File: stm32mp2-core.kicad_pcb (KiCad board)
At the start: 2 copper layers, 2 parts, among them U1 STM32MP257FAI3, U2 MT53E1G32D2FW-046 IT:B

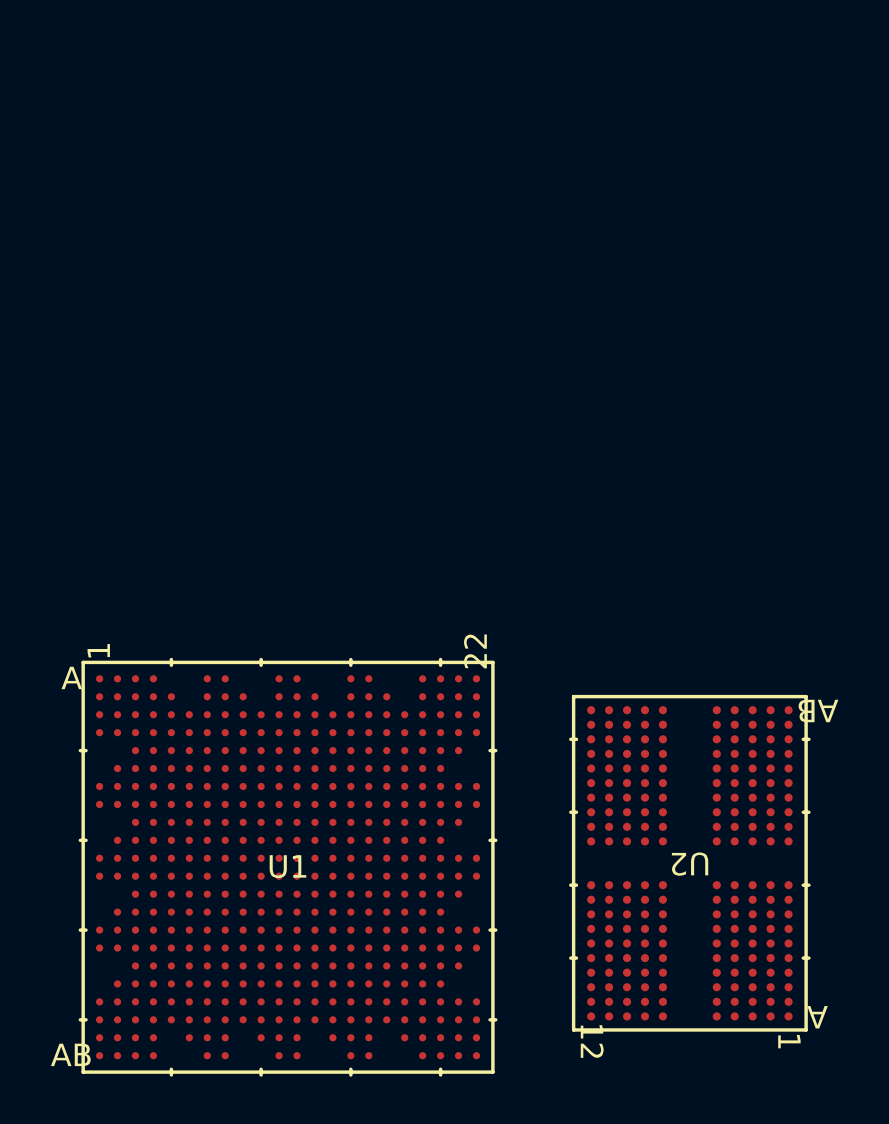
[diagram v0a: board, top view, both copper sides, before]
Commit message: added sd card holder for fun
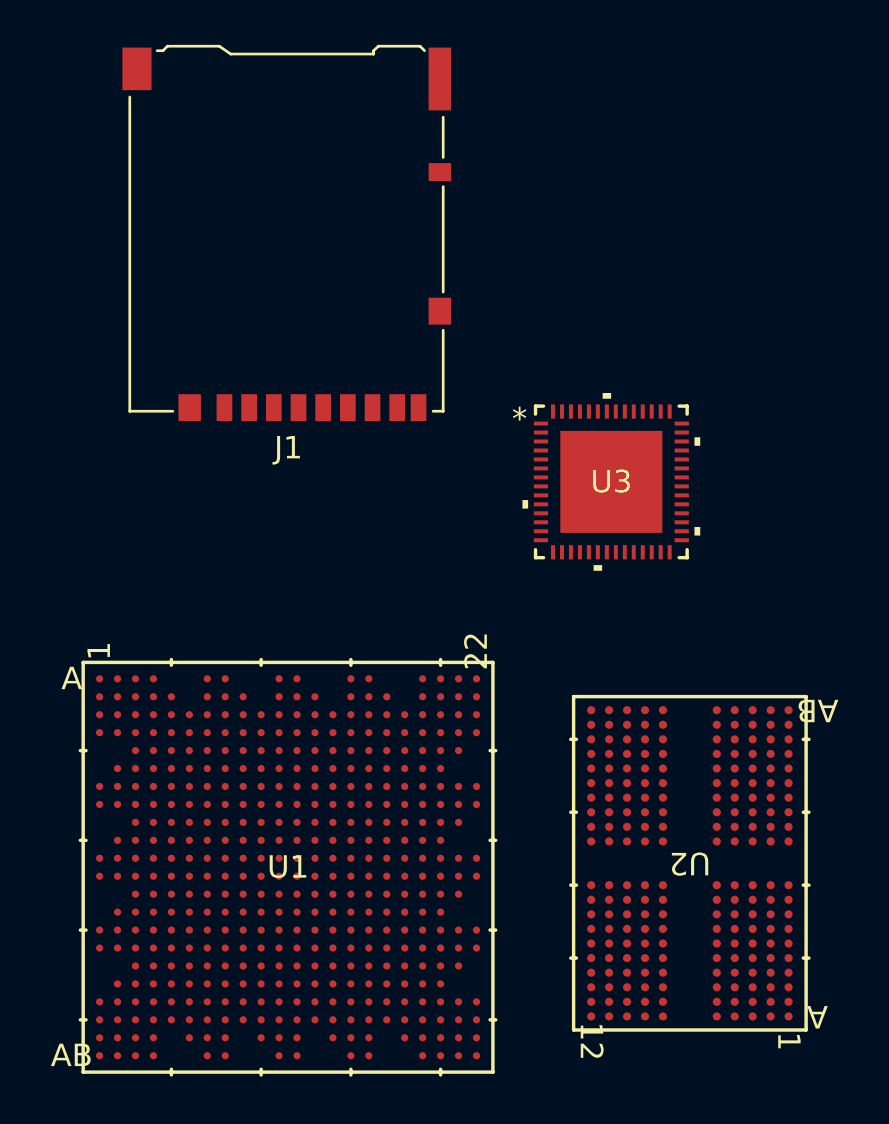
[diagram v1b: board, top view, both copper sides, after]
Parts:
- added J1: Micro_SD_Card_Det1, Connector_Card:microSD_HC_Hirose_DM3AT-SF-PEJM5, F.Cu at (140.0, 61.0)
- added U3: STPMIC25APQR, STPMIC25APQR:WFQFN56L_6p5x6p5x0p9_STM-L, F.Cu at (154.5, 72.0)
